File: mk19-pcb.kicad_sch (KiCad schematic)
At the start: 100 parts, among them J1 Conn_01x02_Socket, J10 Conn_01x02_Socket, J11 Conn_01x02_Socket, J2 Conn_01x02_Socket, J4 Conn_01x02_Socket, J7 Conn_01x02_Socket, J9 Conn_01x02_Socket, P1 FH26W-13S-0_3SHW(60), P10 FH26W-13S-0_3SHW(60), P11 FH26W-13S-0_3SHW(60), P2 FH26W-13S-0_3SHW(60), P3 FH26W-13S-0_3SHW(60), P4 FH26W-13S-0_3SHW(60), P5 FH26W-13S-0_3SHW(60), P6 FH26W-13S-0_3SHW(60), P7 FH26W-13S-0_3SHW(60), P8 FH26W-13S-0_3SHW(60), P9 FH26W-13S-0_3SHW(60), T1 Conn_01x01_Socket, T10 Conn_01x01_Socket, U1 AZC199-04S-MS, U10 8_01A0_008200, U11 8_01A0_008200, U2 1N4148W_C81598, U3 1N4148W_C81598, U4 1N4148W_C81598, U5 1N4148W_C81598, U6 1N4148W_C81598, U7 HC-FPC-05-10-16RLTAG, U8 ECT818001569, U9 8_01A0_008200

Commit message: more minor fixes
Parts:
- added LOGO7: **REF, ct-kicad:cyboard-logo-10mm, symbol ct-kicad:cyboard-logo-10mm
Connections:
- net SPARE_1 is gone; now on net LCD_RST: U11.5
- net SPARE_2 is gone; now on net LCD_DC: U11.6
- net SPARE_3 is gone; now on net LCD3_CS: U11.7
- net SPARE_4 is gone; now on net LCD_BL: U11.8
- net GPIO3 renamed LCD3_CS
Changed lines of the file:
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@@
     (stroke (width 0) (type default))
   )
-  (wire (pts (xy 153.67 354.33) (xy 157.48 354.33))
+  (wire (pts (xy 153.67 351.79) (xy 157.48 351.79))
     (stroke (width 0) (type default))
   )
@@
     (stroke (width 0) (type default))
   )
+  (wire (pts (xy 153.67 354.33) (xy 157.48 354.33))
+    (stroke (width 0) (type default))
+  )
   (wire (pts (xy 784.86 204.47) (xy 784.86 205.74))
     (stroke (width 0) (type default))
@@
     (stroke (width 0) (type default))
   )
-  (wire (pts (xy 153.67 356.87) (xy 157.48 356.87))
-    (stroke (width 0) (type default))
-  )
   (wire (pts (xy 690.88 182.88) (xy 692.15 182.88))
     (stroke (width 0) (type default))
@@
     (stroke (width 0) (type default))
   )
+  (wire (pts (xy 153.67 356.87) (xy 157.48 356.87))
+    (stroke (width 0) (type default))
+  )
   (wire (pts (xy 435.61 250.19) (xy 439.42 250.19))
     (stroke (width 0) (type default))
@@
     (stroke (width 0) (type default))
   )
-  (wire (pts (xy 153.67 351.79) (xy 157.48 351.79))
-    (stroke (width 0) (type default))
-  )
   (wire (pts (xy 193.04 148.59) (xy 193.04 162.56))
     (stroke (width 0) (type default))
@@
     (stroke (width 0) (type default))
   )
+  (wire (pts (xy 153.67 349.25) (xy 157.48 349.25))
+    (stroke (width 0) (type default))
+  )
   (wire (pts (xy 81.28 60.96) (xy 81.28 62.23))
     (stroke (width 0) (type default))
@@
     (stroke (width 0) (type default))
   )
-  (wire (pts (xy 153.67 349.25) (xy 157.48 349.25))
-    (stroke (width 0) (type default))
-  )
   (wire (pts (xy 153.67 361.95) (xy 157.48 361.95))
     (stroke (width 0) (type default))
@@
     (fill (type none))
   )
-  (rectangle (start 19.05 322.58) (end 186.69 392.43)
+  (rectangle (start 19.05 322.58) (end 207.01 392.43)
     (stroke (width 0) (type default))
     (fill (type none))
@@
     (effects (font (face "Futura") (size 1.27 1.27)) (justify left top))
   )
-  (text_box "Spare SPI port"
+  (text_box "Spare SPI TFT port"
     (at 139.7 335.28 0) (size 30.48 3.81)
     (stroke (width 0) (type default))
@@
     (effects (font (size 1.27 1.27)) (justify left bottom))
   )
-  (global_label "GPIO3" (shape output) (at 345.44 48.26 180) (fields_autoplaced)
+  (global_label "LCD3_CS" (shape output) (at 345.44 48.26 180) (fields_autoplaced)
     (effects (font (size 1.27 1.27)) (justify right))
-    (property "Intersheetrefs" "${INTERSHEET_REFS}" (at 336.77 48.26 0)
+    (property "Intersheetrefs" "${INTERSHEET_REFS}" (at 334.2301 48.26 0)
       (effects (font (size 1.27 1.27)) (justify right) hide)
     )
@@
     )
   )
-  (global_label "SPARE_2" (shape input) (at 157.48 354.33 0) (fields_autoplaced)
-    (effects (font (size 1.27 1.27)) (justify left))
-    (property "Intersheetrefs" "${INTERSHEET_REFS}" (at 168.6294 354.33 0)
-      (effects (font (size 1.27 1.27)) (justify left) hide)
-    )
-  )
   (global_label "row6" (shape input) (at 78.74 81.28 0) (fields_autoplaced)
     (effects (font (size 1.27 1.27)) (justify left))
@@
     )
   )
-  (global_label "col2_to_both_bundles" (shape output) (at 758.19 102.87 0) (fields_autoplaced)
+  (global_label "LCD_RST" (shape input) (at 157.48 356.87 0) (fields_autoplaced)
     (effects (font (size 1.27 1.27)) (justify left))
-    (property "Intersheetrefs" "${INTERSHEET_REFS}" (at 781.6156 102.87 0)
+    (property "Intersheetrefs" "${INTERSHEET_REFS}" (at 168.448 356.87 0)
       (effects (font (size 1.27 1.27)) (justify left) hide)
     )
   )
-  (global_label "SPARE_3" (shape input) (at 157.48 351.79 0) (fields_autoplaced)
+  (global_label "col2_to_both_bundles" (shape output) (at 758.19 102.87 0) (fields_autoplaced)
     (effects (font (size 1.27 1.27)) (justify left))
-    (property "Intersheetrefs" "${INTERSHEET_REFS}" (at 168.6294 351.79 0)
+    (property "Intersheetrefs" "${INTERSHEET_REFS}" (at 781.6156 102.87 0)
       (effects (font (size 1.27 1.27)) (justify left) hide)
     )
@@
     )
   )
+  (global_label "LCD3_CS" (shape input) (at 157.48 351.79 0) (fields_autoplaced)
+    (effects (font (size 1.27 1.27)) (justify left))
+    (property "Intersheetrefs" "${INTERSHEET_REFS}" (at 168.6899 351.79 0)
+      (effects (font (size 1.27 1.27)) (justify left) hide)
+    )
+  )
   (global_label "row8" (shape input) (at 703.58 184.15 270) (fields_autoplaced)
     (effects (font (size 1.27 1.27)) (justify right))
@@
     )
   )
+  (global_label "LCD_BL" (shape input) (at 157.48 349.25 0) (fields_autoplaced)
+    (effects (font (size 1.27 1.27)) (justify left))
+    (property "Intersheetrefs" "${INTERSHEET_REFS}" (at 167.299 349.25 0)
+      (effects (font (size 1.27 1.27)) (justify left) hide)
+    )
+  )
   (global_label "rkjxt-b" (shape output) (at 466.09 168.91 0) (fields_autoplaced)
     (effects (font (size 1.27 1.27)) (justify left))
@@
     )
   )
+  (global_label "LCD_DC" (shape input) (at 157.48 354.33 0) (fields_autoplaced)
+    (effects (font (size 1.27 1.27)) (justify left))
+    (property "Intersheetrefs" "${INTERSHEET_REFS}" (at 167.5409 354.33 0)
+      (effects (font (size 1.27 1.27)) (justify left) hide)
+    )
+  )
   (global_label "Split_Comms_TX-A6" (shape bidirectional) (at 40.64 276.86 180) (fields_autoplaced)
     (effects (font (size 1.27 1.27)) (justify right))
@@
     )
   )
-  (global_label "SPARE_4" (shape input) (at 157.48 349.25 0) (fields_autoplaced)
-    (effects (font (size 1.27 1.27)) (justify left))
-    (property "Intersheetrefs" "${INTERSHEET_REFS}" (at 168.6294 349.25 0)
-      (effects (font (size 1.27 1.27)) (justify left) hide)
-    )
-  )
   (global_label "SPI1_MOSI" (shape input) (at 57.15 359.41 0) (fields_autoplaced)
     (effects (font (size 1.27 1.27)) (justify left))
@@
     )
   )
-  (global_label "SPARE_1" (shape input) (at 157.48 356.87 0) (fields_autoplaced)
-    (effects (font (size 1.27 1.27)) (justify left))
-    (property "Intersheetrefs" "${INTERSHEET_REFS}" (at 168.6294 356.87 0)
-      (effects (font (size 1.27 1.27)) (justify left) hide)
-    )
-  )
   (global_label "col pin" (shape input) (at 651.51 107.95 0) (fields_autoplaced)
     (effects (font (size 1.27 1.27)) (justify left))
@@
         )
       )
+    )
+  )
+  (symbol (lib_id "ct-kicad:cyboard-logo-10mm") (at 496.57 92.71 0) (unit 1)
+    (in_bom no) (on_board yes) (dnp no) (fields_autoplaced)
+    (property "Reference" "LOGO7" (at 499.11 91.44 0)
+      (effects (font (size 1.27 1.27)) (justify left))
+    )
+    (property "Value" "**REF" (at 499.11 93.98 0)
+      (effects (font (size 1.27 1.27)) (justify left))
+    )
+    (property "Footprint" "ct-kicad:cyboard-logo-10mm" (at 496.57 92.71 0)
+      (effects (font (size 1.27 1.27)) hide)
+    )
+    (property "Datasheet" "" (at 496.57 92.71 0)
+      (effects (font (size 1.27 1.27)) hide)
+    )
+    (instances
+      (project "mk19-pcb"
+        (path "/2353ceae-84c1-4f16-856e-bae2658fe2c9"
+          (reference "LOGO7") (unit 1)
+        )
+      )

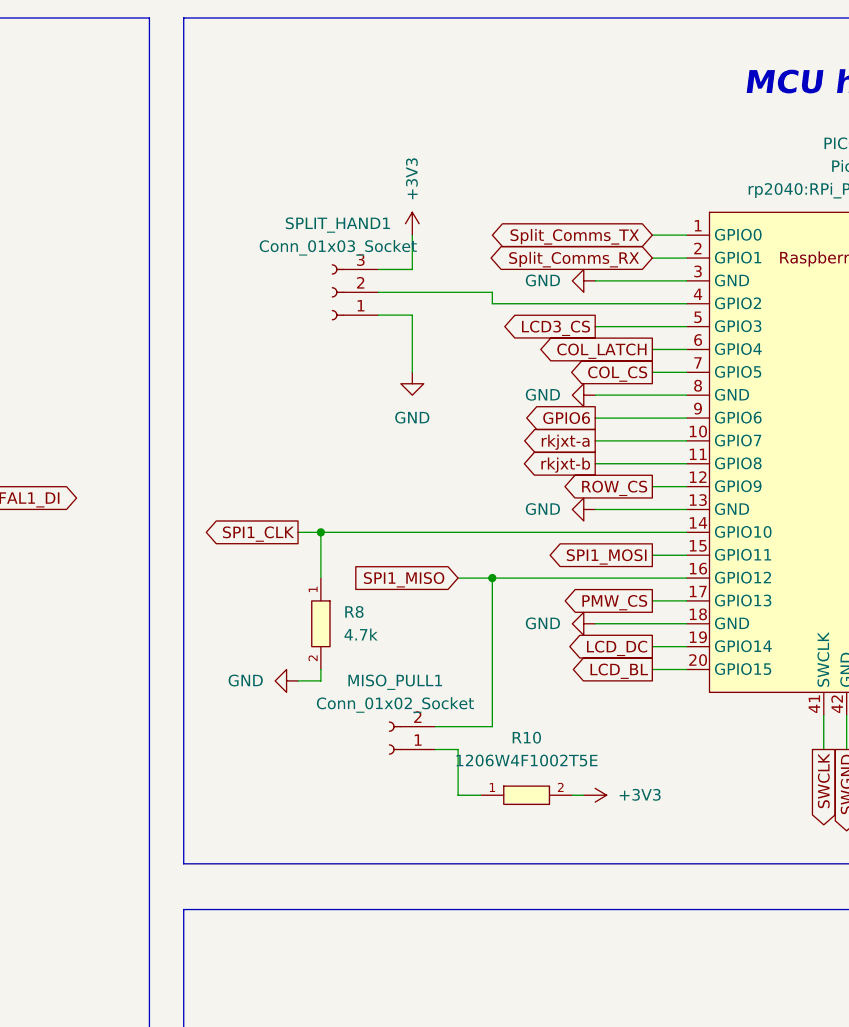
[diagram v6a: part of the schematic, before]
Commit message: adding jumper for clk pulldown
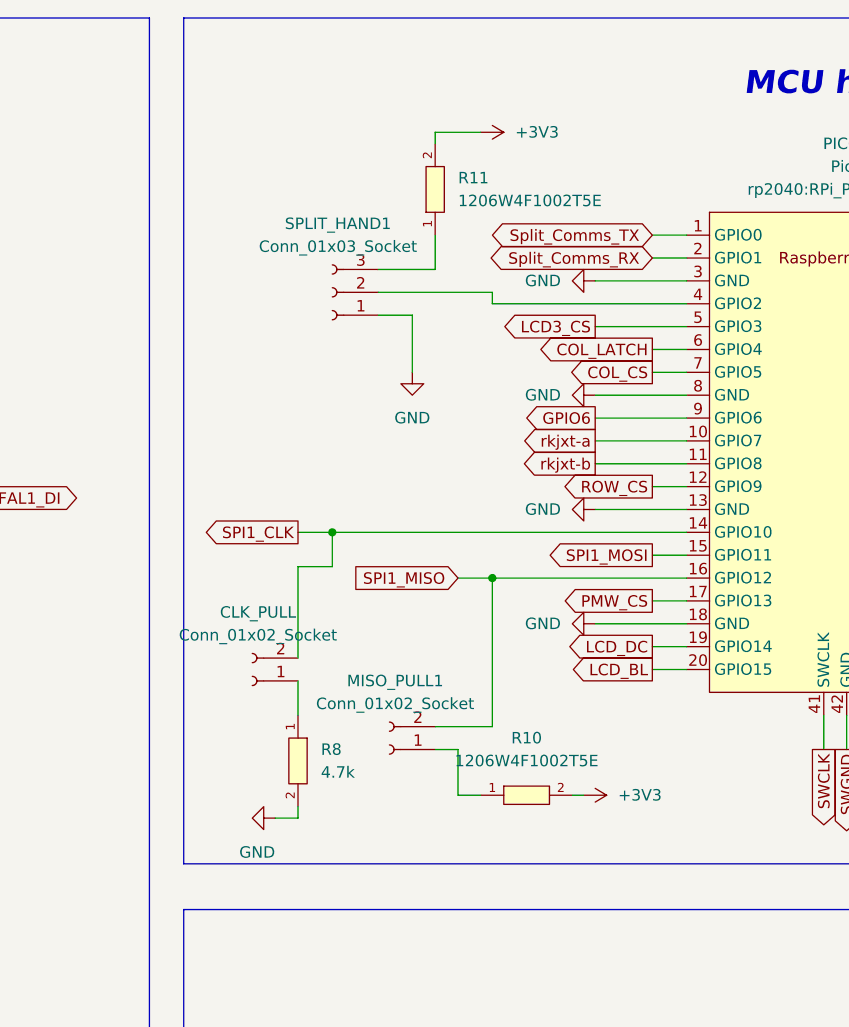
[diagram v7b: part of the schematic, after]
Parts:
- added CLK_PULL: Conn_01x02_Socket, Connector_PinSocket_2.54mm:PinSocket_1x02_P2.54mm_Vertical, symbol Connector:Conn_01x02_Socket
- added R11: 1206W4F1002T5E, ct-kicad:R1206, symbol ct-kicad:1206W4F1002T5E
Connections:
- net +3V3: now also R11.2; no longer SPLIT_HAND1.3 (Pin_3)
- net SPI1_CLK: now also CLK_PULL.2 (Pin_2); no longer R8.1
- new net: R11.1, SPLIT_HAND1.3 (Pin_3)
- new net: CLK_PULL.1 (Pin_1), R8.1
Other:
- moved on the sheet: R8
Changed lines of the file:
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@@
   (junction (at 697.23 205.74) (diameter 0) (color 0 0 0 0)
   )
+  (junction (at 316.23 71.12) (diameter 0) (color 0 0 0 0)
+  )
   (junction (at 135.89 180.34) (diameter 0) (color 0 0 0 0)
   )
@@
   (junction (at 59.69 68.58) (diameter 0) (color 0 0 0 0)
   )
-  (junction (at 314.96 71.12) (diameter 0) (color 0 0 0 0)
-  )
   (junction (at 212.09 143.51) (diameter 0) (color 0 0 0 0)
   )
@@
     (stroke (width 0) (type default))
   )
+  (wire (pts (xy 327.66 26.67) (xy 332.74 26.67))
+    (stroke (width 0) (type default))
+  )
   (wire (pts (xy 444.5 153.67) (xy 452.12 153.67))
     (stroke (width 0) (type default))
@@
     (stroke (width 0) (type default))
   )
+  (wire (pts (xy 312.42 85.09) (xy 312.42 74.93))
+    (stroke (width 0) (type default))
+  )
   (wire (pts (xy 775.97 181.61) (xy 775.97 193.04))
     (stroke (width 0) (type default))
@@
     (stroke (width 0) (type default))
   )
+  (wire (pts (xy 312.42 87.63) (xy 312.42 91.44))
+    (stroke (width 0) (type default))
+  )
   (wire (pts (xy 76.2 68.58) (xy 77.47 68.58))
     (stroke (width 0) (type default))
@@
     (stroke (width 0) (type default))
   )
-  (wire (pts (xy 314.96 86.36) (xy 314.96 87.63))
+  (wire (pts (xy 312.42 101.6) (xy 312.42 102.87))
     (stroke (width 0) (type default))
   )
@@
     (stroke (width 0) (type default))
   )
-  (wire (pts (xy 321.31 41.91) (xy 325.12 41.91))
+  (wire (pts (xy 321.31 41.91) (xy 327.66 41.91))
     (stroke (width 0) (type default))
   )
@@
     (stroke (width 0) (type default))
   )
-  (wire (pts (xy 314.96 71.12) (xy 355.6 71.12))
-    (stroke (width 0) (type default))
-  )
   (wire (pts (xy 692.15 182.88) (xy 692.15 184.15))
     (stroke (width 0) (type default))
@@
     (stroke (width 0) (type default))
   )
+  (wire (pts (xy 327.66 27.94) (xy 327.66 26.67))
+    (stroke (width 0) (type default))
+  )
   (wire (pts (xy 143.51 372.11) (xy 156.21 372.11))
     (stroke (width 0) (type default))
@@
     (stroke (width 0) (type default))
   )
+  (wire (pts (xy 327.66 38.1) (xy 327.66 41.91))
+    (stroke (width 0) (type default))
+  )
   (wire (pts (xy 153.67 361.95) (xy 157.48 361.95))
     (stroke (width 0) (type default))
@@
     (stroke (width 0) (type default))
   )
+  (wire (pts (xy 316.23 71.12) (xy 355.6 71.12))
+    (stroke (width 0) (type default))
+  )
   (wire (pts (xy 207.01 138.43) (xy 207.01 162.56))
     (stroke (width 0) (type default))
@@
     (stroke (width 0) (type default))
   )
-  (wire (pts (xy 312.42 87.63) (xy 314.96 87.63))
+  (wire (pts (xy 309.88 102.87) (xy 312.42 102.87))
     (stroke (width 0) (type default))
   )
@@
     (stroke (width 0) (type default))
   )
+  (wire (pts (xy 312.42 74.93) (xy 316.23 74.93))
+    (stroke (width 0) (type default))
+  )
   (wire (pts (xy 420.37 213.36) (xy 426.72 213.36))
     (stroke (width 0) (type default))
@@
     (stroke (width 0) (type default))
   )
-  (wire (pts (xy 312.42 71.12) (xy 314.96 71.12))
+  (wire (pts (xy 312.42 71.12) (xy 316.23 71.12))
+    (stroke (width 0) (type default))
+  )
+  (wire (pts (xy 316.23 74.93) (xy 316.23 71.12))
     (stroke (width 0) (type default))
   )
@@
     (stroke (width 0) (type default))
   )
-  (wire (pts (xy 314.96 71.12) (xy 314.96 76.2))
-    (stroke (width 0) (type default))
-  )
   (wire (pts (xy 478.79 285.75) (xy 483.87 285.75))
     (stroke (width 0) (type default))
@@
     (stroke (width 0) (type default))
   )
-  (wire (pts (xy 325.12 38.1) (xy 325.12 41.91))
-    (stroke (width 0) (type default))
-  )
   (wire (pts (xy 102.87 354.33) (xy 106.68 354.33))
     (stroke (width 0) (type default))
@@
     )
   )
-  (symbol (lib_id "power:GND") (at 312.42 87.63 270) (unit 1)
-    (in_bom yes) (on_board yes) (dnp no) (fields_autoplaced)
-    (property "Reference" "#PWR0142" (at 306.07 87.63 0)
+  (symbol (lib_id "power:GND") (at 309.88 102.87 270) (unit 1)
+    (in_bom yes) (on_board yes) (dnp no)
+    (property "Reference" "#PWR0142" (at 303.53 102.87 0)
       (effects (font (size 1.27 1.27)) hide)
     )
-    (property "Value" "GND" (at 308.61 87.63 90)
+    (property "Value" "GND" (at 309.88 106.68 90)
       (effects (font (size 1.27 1.27)) (justify right))
     )
-    (property "Footprint" "" (at 312.42 87.63 0)
+    (property "Footprint" "" (at 309.88 102.87 0)
       (effects (font (size 1.27 1.27)) hide)
     )
-    (property "Datasheet" "" (at 312.42 87.63 0)
+    (property "Datasheet" "" (at 309.88 102.87 0)
       (effects (font (size 1.27 1.27)) hide)
     )
@@
     )
   )
+  (symbol (lib_id "Connector:Conn_01x02_Socket") (at 307.34 87.63 180) (unit 1)
+    (in_bom yes) (on_board yes) (dnp no) (fields_autoplaced)
+    (property "Reference" "CLK_PULL" (at 307.975 80.01 0)
+      (effects (font (size 1.27 1.27)))
+    )
+    (property "Value" "Conn_01x02_Socket" (at 307.975 82.55 0)
+      (effects (font (size 1.27 1.27)))
+    )
+    (property "Footprint" "Connector_PinSocket_2.54mm:PinSocket_1x02_P2.54mm_Vertical" (at 307.34 87.63 0)
+      (effects (font (size 1.27 1.27)) hide)
+    )
+    (property "Datasheet" "~" (at 307.34 87.63 0)
+      (effects (font (size 1.27 1.27)) hide)
+    )
+    (pin "1")
+    (pin "2")
+    (instances
+      (project "mk19-pcb"
+        (path "/2353ceae-84c1-4f16-856e-bae2658fe2c9"
+          (reference "CLK_PULL") (unit 1)
+        )
+      )
+    )
+  )
   (symbol (lib_id "Connector:Conn_01x01_Socket") (at 520.7 292.1 180) (unit 1)
     (in_bom no) (on_board yes) (dnp no) (fields_autoplaced)
@@
     )
   )
-  (symbol (lib_id "power:+3V3") (at 325.12 38.1 0) (unit 1)
+  (symbol (lib_id "power:+3V3") (at 332.74 26.67 270) (unit 1)
     (in_bom yes) (on_board yes) (dnp no)
-    (property "Reference" "#PWR042" (at 325.12 41.91 0)
+    (property "Reference" "#PWR042" (at 328.93 26.67 0)
       (effects (font (size 1.27 1.27)) hide)
     )
-    (property "Value" "+3V3" (at 325.12 34.29 90)
+    (property "Value" "+3V3" (at 336.55 26.67 90)
       (effects (font (size 1.27 1.27)) (justify left))
     )
-    (property "Footprint" "" (at 325.12 38.1 0)
+    (property "Footprint" "" (at 332.74 26.67 0)
       (effects (font (size 1.27 1.27)) hide)
     )
-    (property "Datasheet" "" (at 325.12 38.1 0)
+    (property "Datasheet" "" (at 332.74 26.67 0)
       (effects (font (size 1.27 1.27)) hide)
     )
@@
     )
   )
+  (symbol (lib_id "ct-kicad:1206W4F1002T5E") (at 327.66 33.02 90) (unit 1)
+    (in_bom yes) (on_board yes) (dnp no) (fields_autoplaced)
+    (property "Reference" "R11" (at 330.2 31.75 90)
+      (effects (font (size 1.27 1.27)) (justify right))
+    )
+    (property "Value" "1206W4F1002T5E" (at 330.2 34.29 90)
+      (effects (font (size 1.27 1.27)) (justify right))
+    )
+    (property "Footprint" "ct-kicad:R1206" (at 337.82 33.02 0)
+      (effects (font (size 1.27 1.27) italic) hide)
+    )
+    (property "Datasheet" "https://item.szlcsc.com/311874.html" (at 327.533 35.306 0)
+      (effects (font (size 1.27 1.27)) (justify left) hide)
+    )
+    (property "LCSC" "C17902" (at 327.66 33.02 0)
+      (effects (font (size 1.27 1.27)) hide)
+    )
+    (pin "1")
+    (pin "2")
+    (instances
+      (project "mk19-pcb"
+        (path "/2353ceae-84c1-4f16-856e-bae2658fe2c9"
+          (reference "R11") (unit 1)
+        )
+      )
+    )
+  )
   (symbol (lib_id "Connector:Conn_01x03_Socket") (at 474.98 320.04 180) (unit 1)
     (in_bom no) (on_board yes) (dnp no) (fields_autoplaced)
@@
     )
   )
-  (symbol (lib_id "ct-kicad:1206W4F1002T5E") (at 314.96 81.28 270) (unit 1)
+  (symbol (lib_id "ct-kicad:1206W4F1002T5E") (at 312.42 96.52 270) (unit 1)
     (in_bom yes) (on_board yes) (dnp no) (fields_autoplaced)
-    (property "Reference" "R8" (at 317.5 80.01 90)
+    (property "Reference" "R8" (at 314.96 95.25 90)
       (effects (font (size 1.27 1.27)) (justify left))
     )
-    (property "Value" "4.7k" (at 317.5 82.55 90)
+    (property "Value" "4.7k" (at 314.96 97.79 90)
       (effects (font (size 1.27 1.27)) (justify left))
     )
-    (property "Footprint" "ct-kicad:R1206" (at 304.8 81.28 0)
+    (property "Footprint" "ct-kicad:R1206" (at 302.26 96.52 0)
       (effects (font (size 1.27 1.27) italic) hide)
     )
-    (property "Datasheet" "https://item.szlcsc.com/311874.html" (at 315.087 78.994 0)
+    (property "Datasheet" "https://item.szlcsc.com/311874.html" (at 312.547 94.234 0)
       (effects (font (size 1.27 1.27)) (justify left) hide)
     )
-    (property "LCSC" "C17902" (at 314.96 81.28 0)
+    (property "LCSC" "C17902" (at 312.42 96.52 0)
       (effects (font (size 1.27 1.27)) hide)
     )
